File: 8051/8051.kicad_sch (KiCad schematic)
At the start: 31 parts, among them J1 GND, J10 C_{OUT}, J2 V_{CC}, J3 OUT TX RX V5 G, J4 S + G, J5 G + CK D, J6 AP-B-C, J7 AN-B-C, J8 A_{OUT}, J9 B_{OUT}, U1 L7805, U2 REGULAR-7133-1, U3 C8051F330

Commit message: digital module
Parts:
- removed J1: GND, MountingHole:MountingHole_2.5mm_Pad_TopBottom, symbol Connector_Generic:Conn_01x01
- removed J10: C_{OUT}, MountingHole:MountingHole_2.5mm_Pad_TopBottom, symbol Connector_Generic:Conn_01x01
- removed J2: V_{CC}, MountingHole:MountingHole_2.5mm_Pad_TopBottom, symbol Connector_Generic:Conn_01x01
- removed J6: AP-B-C, footprint:CONN3-P2.54-DR1.0-W1.5, symbol Connector_Generic:Conn_01x03
- removed J7: AN-B-C, footprint:CONN3-P2.54-DR1.0-W1.5, symbol Connector_Generic:Conn_01x03
- removed J8: A_{OUT}, MountingHole:MountingHole_2.5mm_Pad_TopBottom, symbol Connector_Generic:Conn_01x01
- removed J9: B_{OUT}, MountingHole:MountingHole_2.5mm_Pad_TopBottom, symbol Connector_Generic:Conn_01x01
- added C5: (no value), symbol Device:C
- added C6, C7: C, footprint:0805_p2.0xpad1.0, symbol Device:C
- added D1: (no value), symbol Device:D
- added D2, D3: D, footprint:0805_p2.0xpad1.0, symbol Device:D
- added J6: (no value), symbol Connector_Generic:Conn_01x11
- added U4: (no value), symbol sch_component:IR2103
- added U5, U6: IR2103, footprint:SOIC-8, symbol sch_component:IR2103
- renumbered J4 to J3, J3 to J4, R8 to R10, R9 to R11, R10 to R12, R11 to R13, R12 to R14, R16 to R3, R17 to R4, R3 to R5, R4 to R6, R5 to R7, R6 to R8, R7 to R9
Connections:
- net AN: now also U4.3 (Lin)
- net AOUT: now also J6.3 (Pin_3), U4.6 (Vs)
- net AP: now also U3.13 (P1.0), U4.2 (Hin); no longer U3.10 (P1.3)
- net BN: now also U5.3 (Lin)
- net BOUT: now also J6.6 (Pin_6), U5.6 (Vs)
- net BP: now also U5.2 (Hin)
- net CN: now also U6.3 (Lin)
- net COUT: now also J6.9 (Pin_9), U6.6 (Vs)
- net CP: now also U3.10 (P1.3), U6.2 (Hin); no longer U3.13 (P1.0)
- net CPOUT: now also U3.19 (P0.2); no longer U3.20 (P0.1)
- net GND: now also J6.11 (Pin_11), U4.4 (COM), U5.4 (COM), U6.4 (COM)
- net RCP: now also U3.20 (P0.1); no longer U3.19 (P0.2)
- net VCC: now also D1.2 (A), D2.2 (A), D3.2 (A), J6.1 (Pin_1), U4.1 (Vcc), U5.1 (Vcc), U6.1 (Vcc)
- new net: C5.1, D1.1 (K), U4.8 (Vb)
- new net: C7.1, D3.1 (K), U6.8 (Vb)
- new net: C6.1, D2.1 (K), U5.8 (Vb)
- new net DAN: J6.4 (Pin_4), U4.5 (Lo)
- new net DAP: C5.2, J6.2 (Pin_2), U4.7 (Ho)
- new net DBN: J6.7 (Pin_7), U5.5 (Lo)
- new net DBP: C6.2, J6.5 (Pin_5), U5.7 (Ho)
- new net DCN: J6.10 (Pin_10), U6.5 (Lo)
- new net DCP: C7.2, J6.8 (Pin_8), U6.7 (Ho)
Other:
- removed sheet Sheet616A663B
- removed sheet Sheet617115BF
- removed sheet Sheet61711659

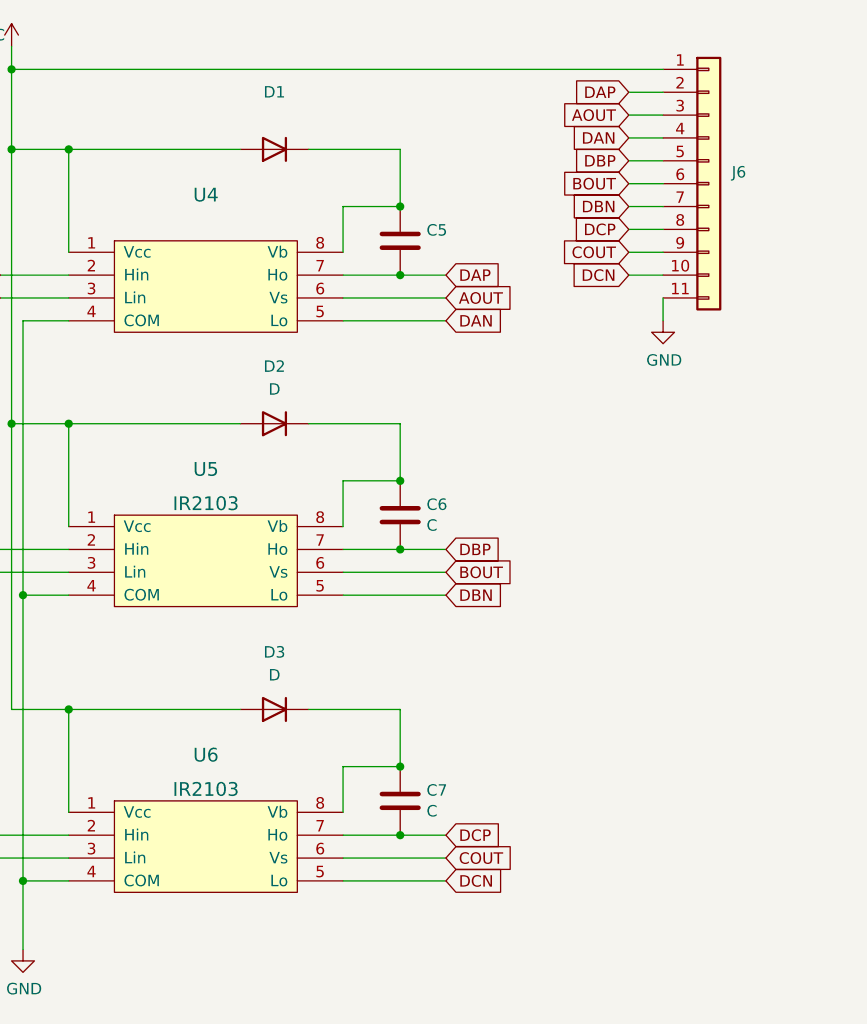
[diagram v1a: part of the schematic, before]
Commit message: 已经打样，但是3伏和5伏的稳压没有做到地的过孔
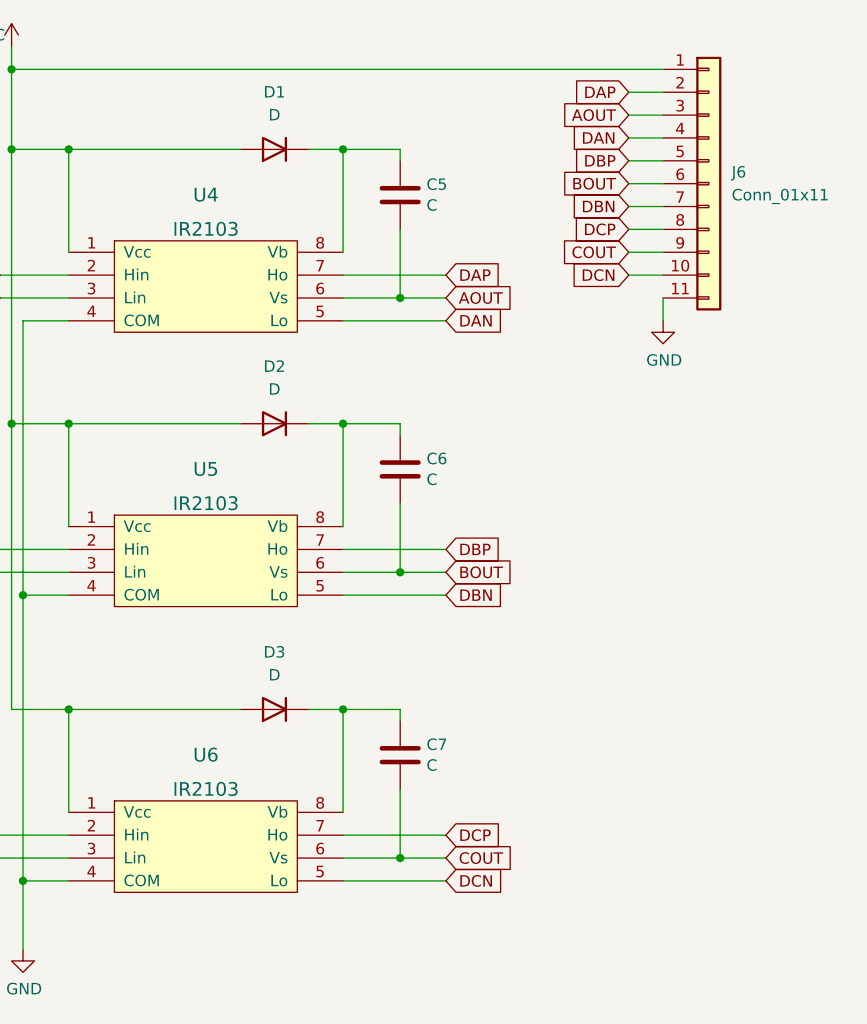
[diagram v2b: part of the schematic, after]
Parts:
- C5: value (none) -> C; footprint (none) -> footprint:0805_p2.0xpad1.0
- D1: value (none) -> D; footprint (none) -> footprint:0805_p2.0xpad1.0
- J6: value (none) -> Conn_01x11; footprint (none) -> Connector_PinHeader_2.54mm:PinHeader_1x11_P2.54mm_Vertical
- U4: value (none) -> IR2103; footprint (none) -> footprint:SOIC-8
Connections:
- net AOUT: now also C5.2
- net BOUT: now also C6.2
- net COUT: now also C7.2
- net DAP: no longer C5.2
- net DBP: no longer C6.2
- net DCP: no longer C7.2
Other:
- moved on the sheet: C5, C6, C7
